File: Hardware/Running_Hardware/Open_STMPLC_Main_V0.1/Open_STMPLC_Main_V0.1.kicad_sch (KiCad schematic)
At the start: 40 parts, among them J1 RJ45_Bel_SI-60062-F, J4 DE9_Pins, J5 TF-102, U1 LAN8720A, U4 ADM2587E, U5 W25Q64JVSSIQ, U6 TPD4E1U06DCKR

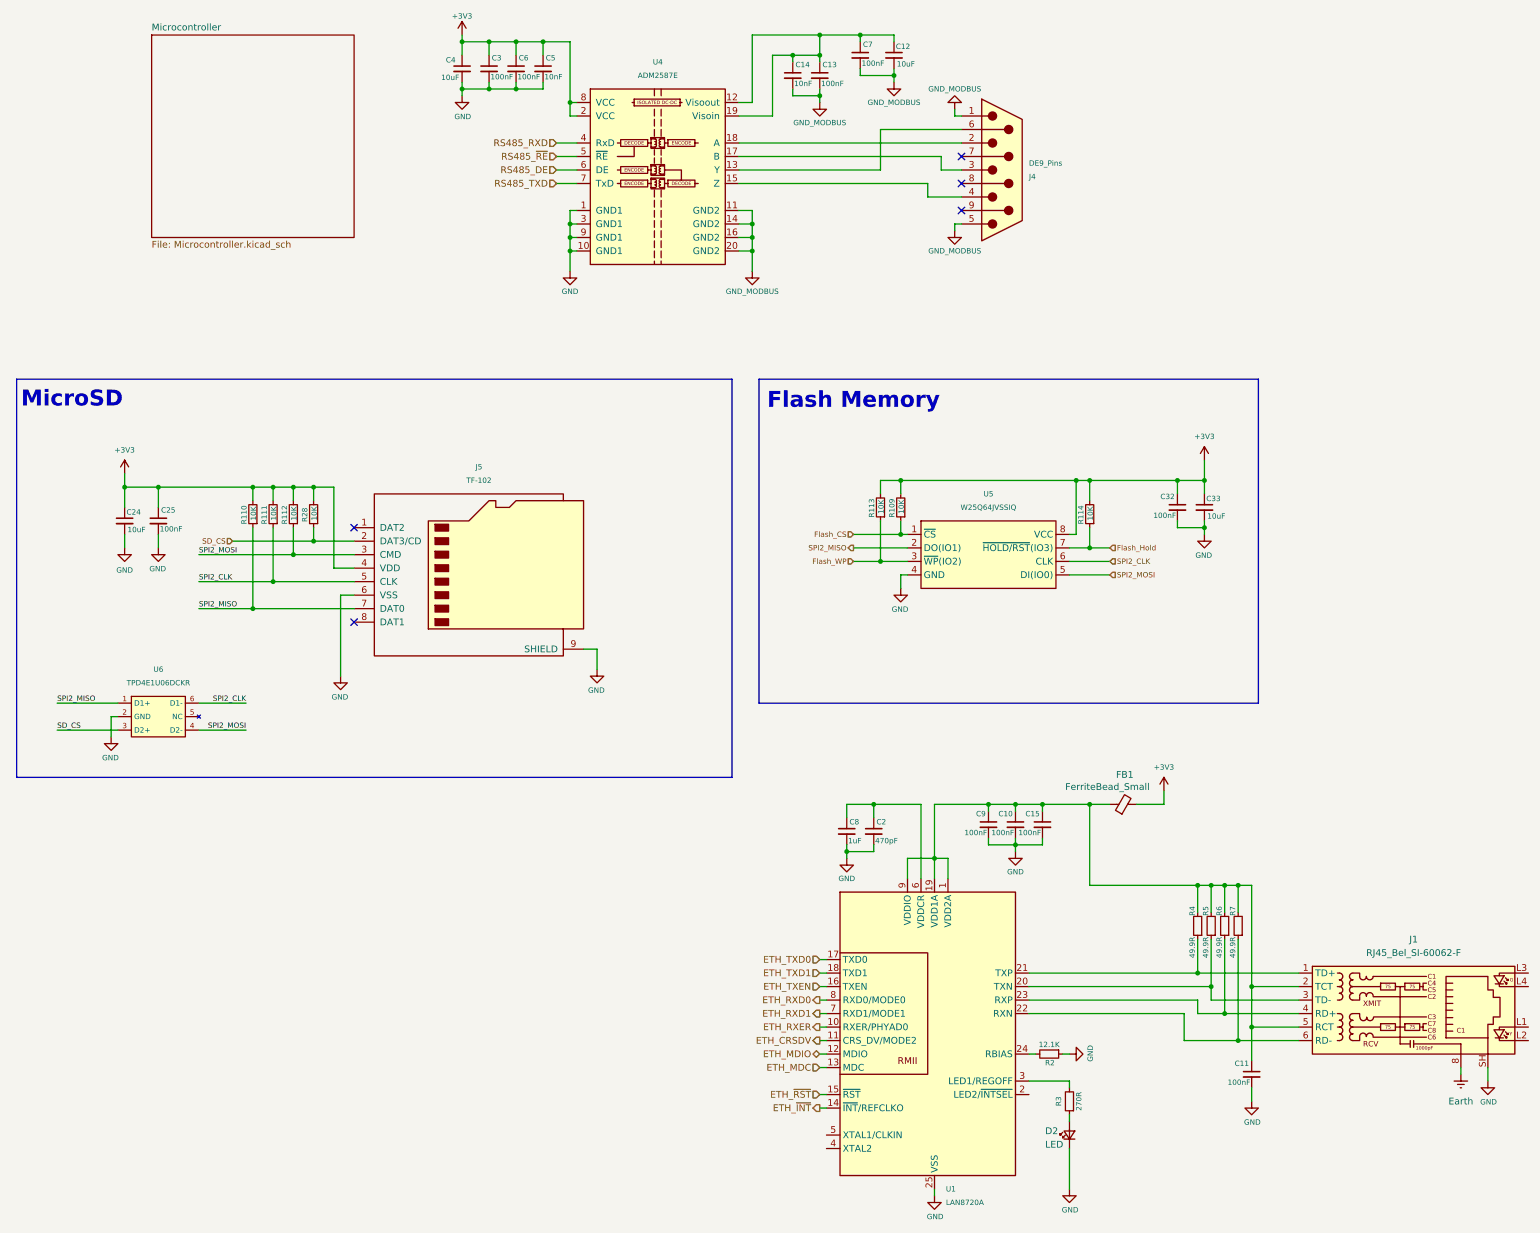
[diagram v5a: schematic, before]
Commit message: IO board schematic changes
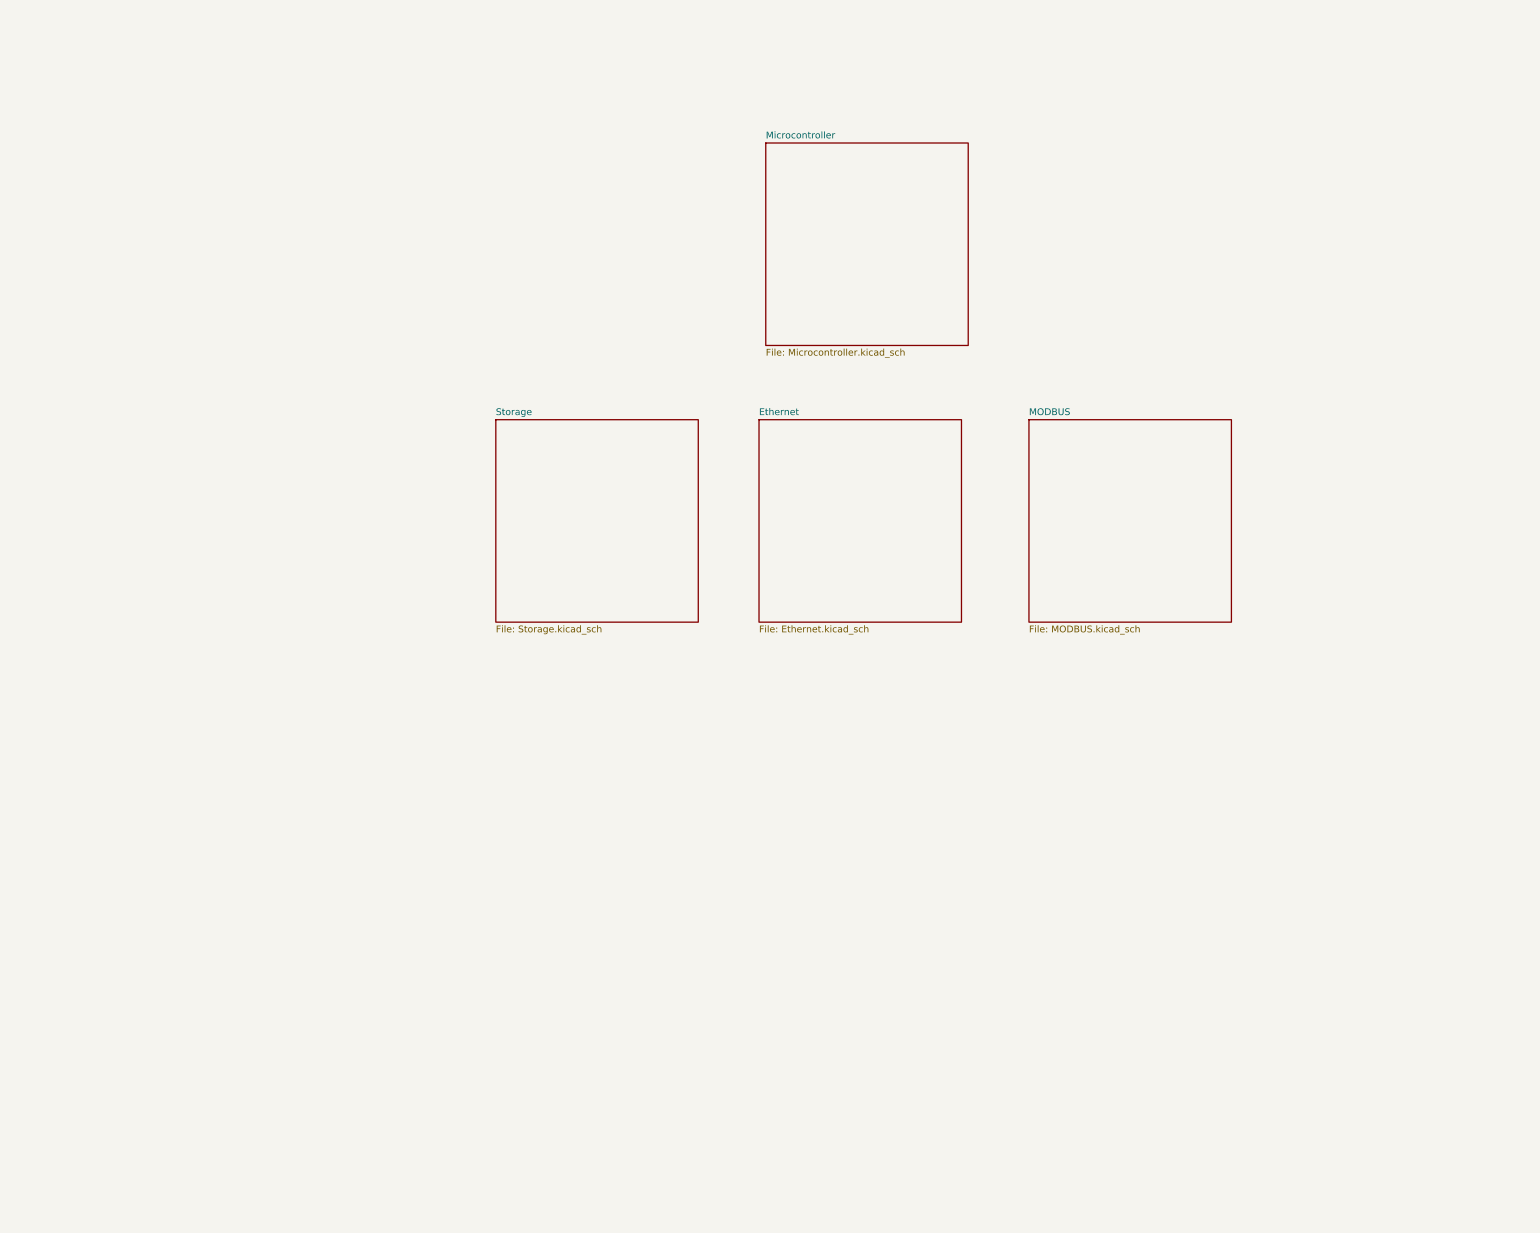
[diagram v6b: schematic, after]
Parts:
- removed C10, C11, C13, C15, C25, C3, C32, C6, C7, C9: 100nF, Capacitor_SMD:C_0603_1608Metric_Pad1.08x0.95mm_HandSolder, symbol Device:C_Small
- removed C12, C24, C33, C4: 10uF, Capacitor_SMD:C_0805_2012Metric_Pad1.18x1.45mm_HandSolder, symbol Device:C_Small
- removed C14, C5: 10nF, Capacitor_SMD:C_0603_1608Metric_Pad1.08x0.95mm_HandSolder, symbol Device:C_Small
- removed C2: 470pF, symbol Device:C_Small
- removed C8: 1uF, symbol Device:C_Small
- removed D2: LED, symbol Device:LED_Small
- removed FB1: FerriteBead_Small, symbol Device:FerriteBead_Small
- removed J1: RJ45_Bel_SI-60062-F, Connector_RJ:RJ45_Bel_SI-60062-F, symbol Connector:RJ45_Bel_SI-60062-F
- removed J4: DE9_Pins, symbol Connector:DE9_Pins
- removed J5: TF-102, Connector_Card:microSD_HC_Molex_47219-2001, symbol Connector:Micro_SD_Card
- removed R109, R110, R111, R112, R113, R114, R28: 10K, Resistor_SMD:R_0603_1608Metric_Pad0.98x0.95mm_HandSolder, symbol Device:R_Small
- removed R2: 12.1K, Resistor_SMD:R_0603_1608Metric_Pad0.98x0.95mm_HandSolder, symbol Device:R_Small
- removed R3: 270R, symbol Device:R_Small
- removed R4, R5, R6, R7: 49.9R, Resistor_SMD:R_0603_1608Metric_Pad0.98x0.95mm_HandSolder, symbol Device:R_Small
- removed U1: LAN8720A, Package_DFN_QFN:VQFN-24-1EP_4x4mm_P0.5mm_EP2.5x2.5mm_ThermalVias, symbol Interface_Ethernet:LAN8720A
- removed U4: ADM2587E, Package_SO:SOIC-20W_7.5x12.8mm_P1.27mm, symbol Interface_UART:ADM2587E
- removed U5: W25Q64JVSSIQ, Package_SO:SOIC-8_5.3x5.3mm_P1.27mm, symbol Flash_Memory:W25Q64JVSSIQ
- removed U6: TPD4E1U06DCKR, Package_TO_SOT_SMD:SOT-363_SC-70-6_Handsoldering, symbol TVS_Diode:TPD4E1U06DCKR
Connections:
- no-connect marks 5 -> 0
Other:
- added sheet Ethernet (Ethernet.kicad_sch)
- added sheet MODBUS (MODBUS.kicad_sch)
- added sheet Storage (Storage.kicad_sch)
- note removed: "Flash Memory"
- note removed: "MicroSD"

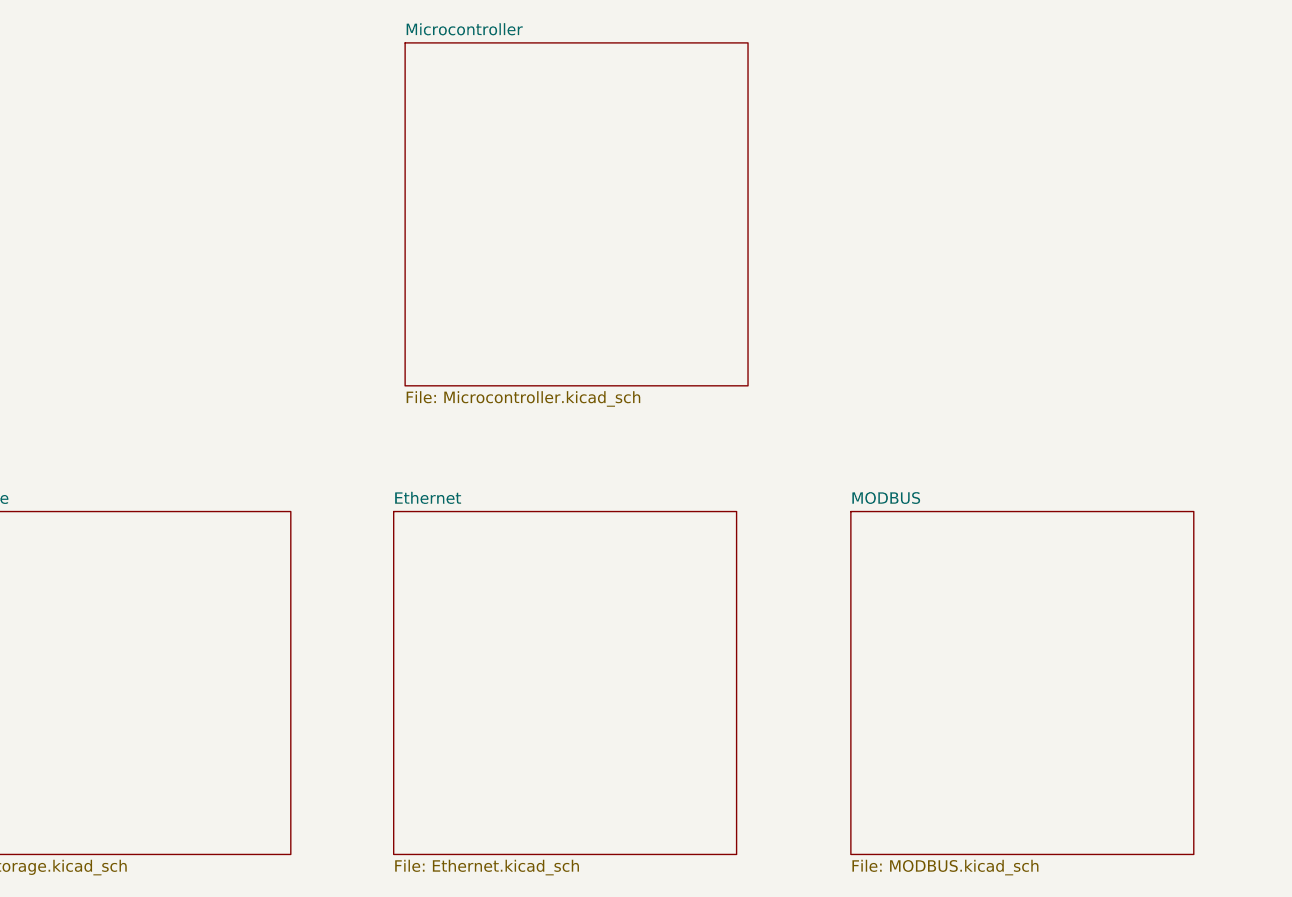
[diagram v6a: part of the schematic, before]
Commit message: GSM Module add
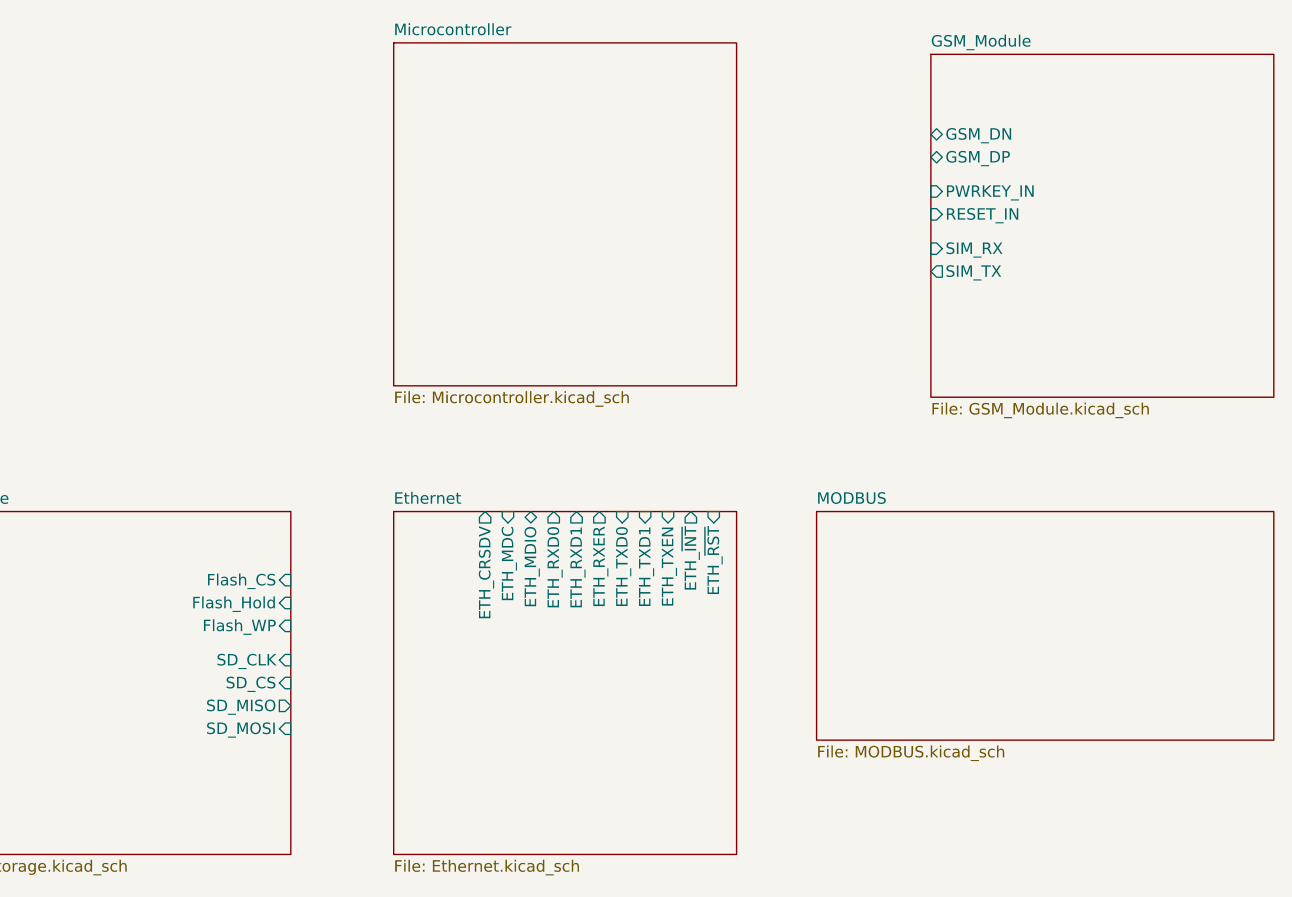
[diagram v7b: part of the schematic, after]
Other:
- added sheet GSM_Module (GSM_Module.kicad_sch)
- sheet Ethernet ports: added ETH_CRSDV, ETH_MDC, ETH_MDIO, ETH_RXD0, ETH_RXD1, ETH_RXER, ETH_TXD0, ETH_TXD1, ETH_TXEN, ETH_~{INT}, ETH_~{RST}; removed none
- sheet Storage ports: added Flash_CS, Flash_Hold, Flash_WP, SD_CLK, SD_CS, SD_MISO, SD_MOSI; removed none
